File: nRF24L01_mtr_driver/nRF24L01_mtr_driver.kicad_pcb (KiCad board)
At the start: 2 copper layers, 77 x 47 mm, 121 parts, among them J1 Micro USB, J2 I/O, J4 VBAT, J5 MTR, J6 SERVO, J7 ICSP, Q1 AO4484, Q2 AO4484, Q3 AO4484, Q4 AO4484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

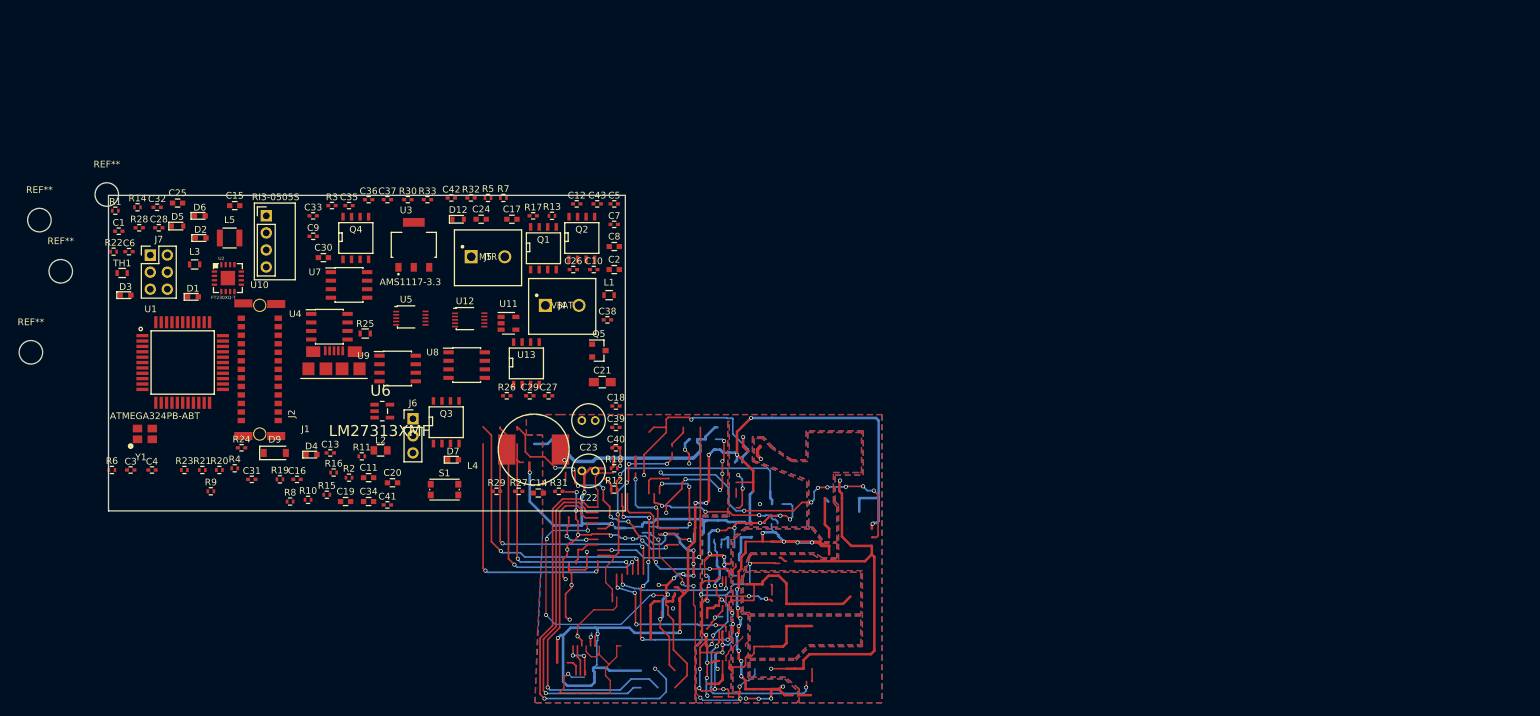
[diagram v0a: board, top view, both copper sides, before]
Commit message: added voltage sense isolation, needs routing
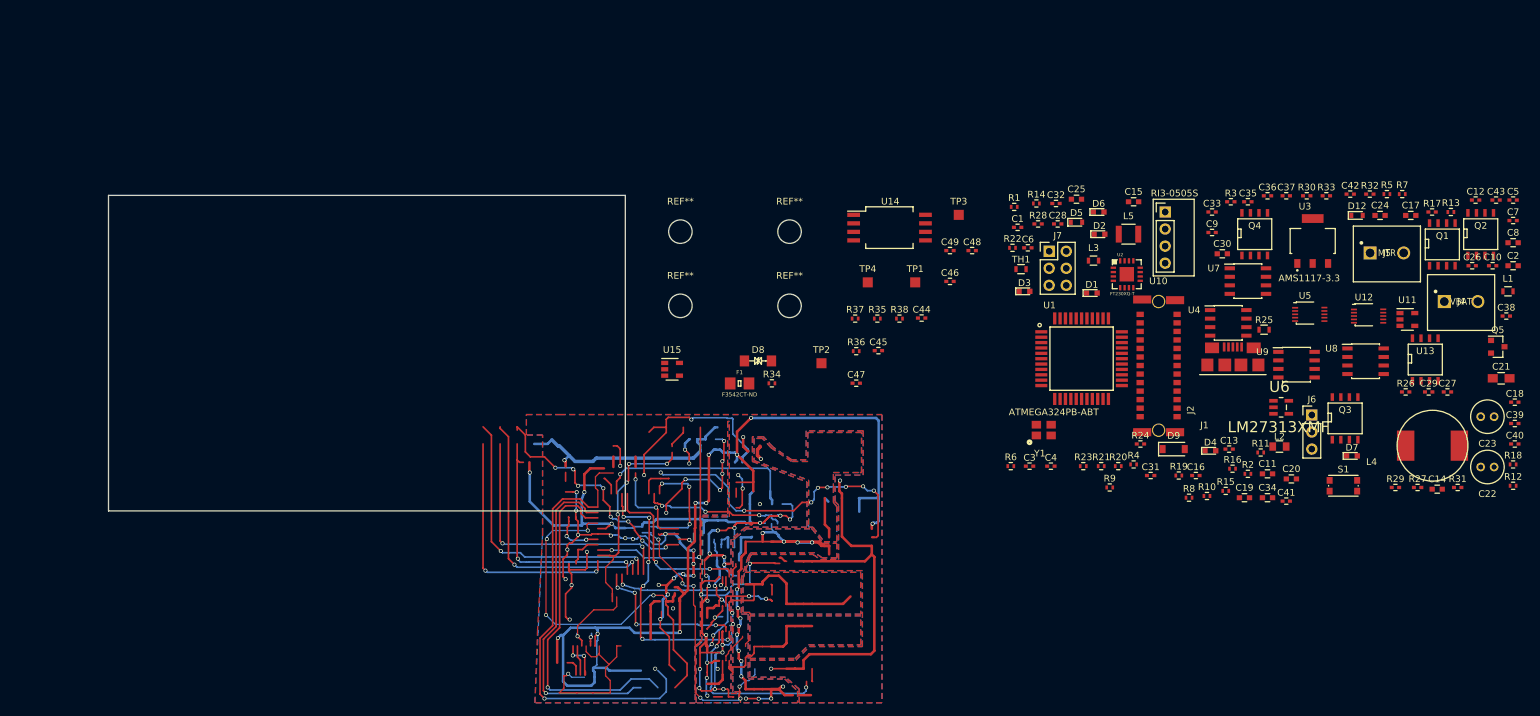
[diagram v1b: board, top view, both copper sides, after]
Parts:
- added C44: .1u, Capacitors_SMD:C_0402, F.Cu at (159.1, 60.7)
- added C45: .1u, Capacitors_SMD:C_0402, F.Cu at (152.6, 65.5)
- added C46: .1u, Capacitors_SMD:C_0402, F.Cu at (163.3, 55.2)
- added C47: .1u, Capacitors_SMD:C_0402, F.Cu at (149.3, 70.4)
- added C48: .1u, Capacitors_SMD:C_0402, F.Cu at (166.6, 50.6)
- added C49: .1u, Capacitors_SMD:C_0402, F.Cu at (163.3, 50.6)
- added D8: SMA6J18AHR3G, mc-footprints:DO-214AC, F.Cu at (132.7, 67.1)
- added F1: F3542CT-ND, Resistors:1206, F.Cu at (132.0, 70.4)
- added R34: 10k, Resistors_SMD:R_0402, F.Cu at (136.8, 70.4)
- added R35: 10k, Resistors_SMD:R_0402, F.Cu at (152.5, 60.8)
- added R36: 10k, Resistors_SMD:R_0402, F.Cu at (149.3, 65.6)
- added R37: 10k, Resistors_SMD:R_0402, F.Cu at (149.2, 60.8)
- added R38: 1k, Resistors_SMD:R_0402, F.Cu at (155.8, 60.8)
- added TP1: 5V0_PWR, Measurement_Points:Measurement_Point_Square-SMD-Pad_Small, F.Cu at (158.1, 55.4)
- added TP2: 12V_PWR, Measurement_Points:Measurement_Point_Square-SMD-Pad_Small, F.Cu at (144.1, 67.4)
- added TP3: 5V0_PWR, Measurement_Points:Measurement_Point_Square-SMD-Pad_Small, F.Cu at (164.6, 45.3)
- added TP4: 3V3_PWR, Measurement_Points:Measurement_Point_Square-SMD-Pad_Small, F.Cu at (151.0, 55.4)
- added U14: ACPL-C87A, Housings_SOIC:SSO-8_6.8x5.9mm_Pitch1.27mm_Clearance8mm, F.Cu at (154.3, 47.2)
- added U15: OPA237_SOT23-5, TO_SOT_Packages_SMD:SOT-23-5, F.Cu at (121.9, 68.3)
- R19: value 10k -> 100k
- R20: value 38k -> 12.7k
- moved C1 133.9 mm to (173.4, 47.2)
- moved C10 133.9 mm to (244.1, 52.9)
- moved C11 133.9 mm to (210.6, 83.9)
- moved C12 133.9 mm to (241.6, 43.1)
- moved C13 133.9 mm to (204.9, 80.2)
- moved C14 133.9 mm to (235.8, 86.2)
- moved C15 133.9 mm to (190.6, 43.4)
- moved C16 133.9 mm to (199.9, 84.1)
- moved C17 133.9 mm to (231.9, 45.4)
- moved C18 133.9 mm to (247.4, 73.2)
- moved C19 133.9 mm to (207.1, 87.4)
- moved C2 133.9 mm to (247.1, 52.9)
- moved C20 133.9 mm to (214.1, 84.6)
- moved C21 133.9 mm to (245.4, 69.7)
- moved C22 133.9 mm to (242.3, 82.9)
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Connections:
- C15 pad 1: /12V -> 12V_PWR
- C25 pad 1: /12V -> 12V_PWR
- C27 pad 1: /ADC1 -> Net-(C27-Pad1)
- C27 pad 2: GNDA -> GND_PWR
- C35 pad 2: /5V_MCU -> 5V0_MCU
- C36 pad 2: /5V_MCU -> 5V0_MCU
- C37 pad 2: /5V_MCU -> 5V0_MCU
- C38 pad 2: /5V_PWR -> 5V0_PWR
- C39 pad 2: /5V_PWR -> 5V0_PWR
- C40 pad 2: /5V_PWR -> 5V0_PWR
- D12 pad 2: /12V -> 12V_PWR
- D5 pad 2: /12V -> 12V_PWR
- J4 pad 1: VBAT -> Net-(F1-Pad2)
- R19 pad 1: /ADC1 -> VBAT
- R19 pad 2: GNDA -> Net-(C27-Pad1)
- R20 pad 1: /VBAT_S -> Net-(C27-Pad1)
- R20 pad 2: /ADC1 -> GND_PWR
- R5 pad 1: /12V -> 12V_PWR
- R6 pad 1: /3.3V -> 3V3_MCU
- R8 pad 1: /5V_mtr_driver -> 5V0_PWR
- U12 pad 1: /12V -> 12V_PWR
- U5 pad 1: /12V -> 12V_PWR
- U7 pad 1: /5V_MCU -> 5V0_MCU
- U7 pad 8: /5V_PWR -> 5V0_PWR
- U8 pad 1: /5V_MCU -> 5V0_MCU
- U8 pad 8: /5V_PWR -> 5V0_PWR
- U9 pad 1: /5V_MCU -> 5V0_MCU
- U9 pad 8: /5V_PWR -> 5V0_PWR
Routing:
- net (no net): track 1540.1 -> 1724.4 mm, vias 172 -> 181
- net Net-(C33-Pad1): track 81.4 -> 0.00 mm, vias 4 -> 0
- net VBAT: track 63.9 -> 0.00 mm, vias 3 -> 0
- net 5V0_PWR: track 35.1 -> 0.00 mm, vias 1 -> 0
- net /5V_PWR: track 3.78 -> 0.00 mm, vias 1 -> 0

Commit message: Changed the footprint of some 0603 cpacitors to 0402 to save space
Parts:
- C20, C30, C8: footprint Capacitors_SMD:C_0603 -> Capacitors_SMD:C_0402
- C21: footprint Capacitors_SMD:C_0805_HandSoldering -> Capacitors_SMD:C_0805
- R25: footprint Resistors_SMD:R_0603 -> Resistors_SMD:R_0402

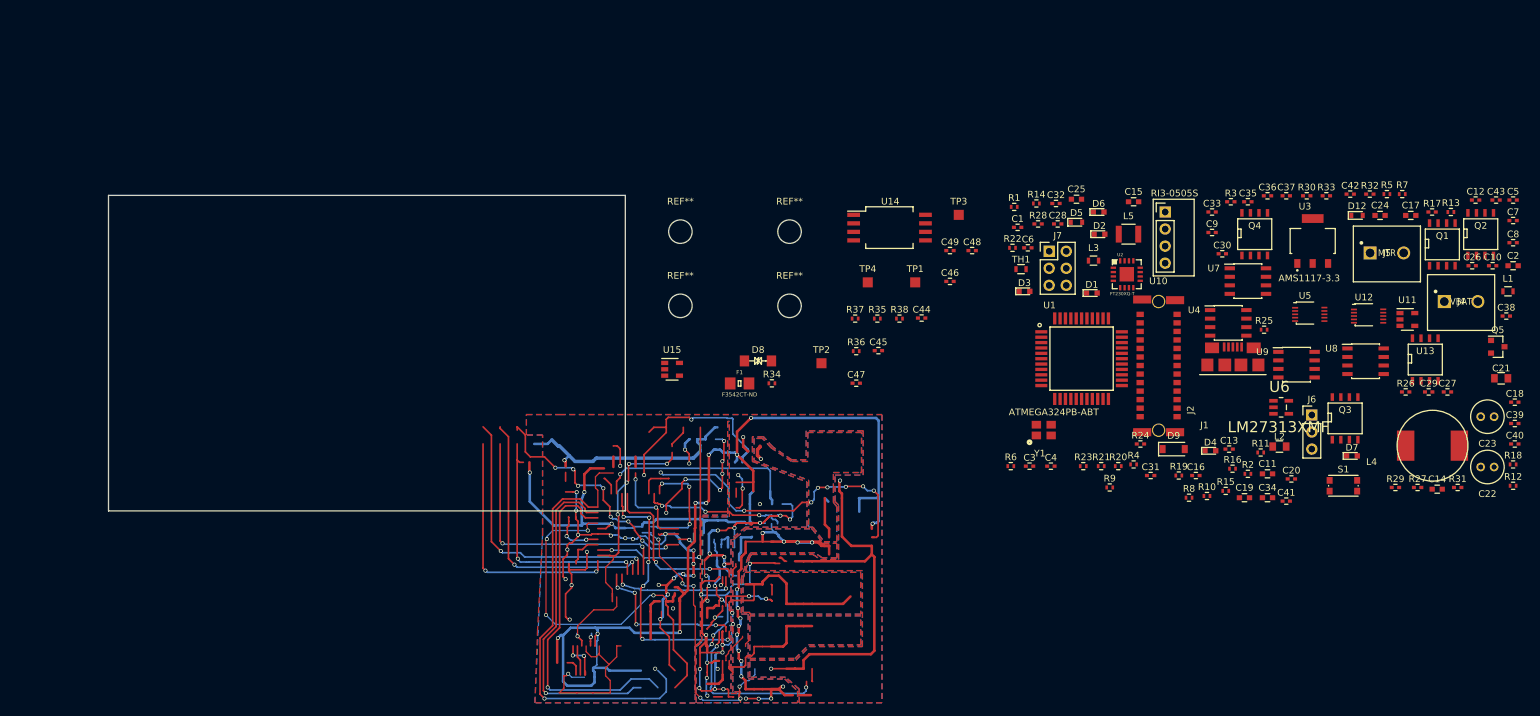
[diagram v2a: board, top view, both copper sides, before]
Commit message: placed major coponents, no routing
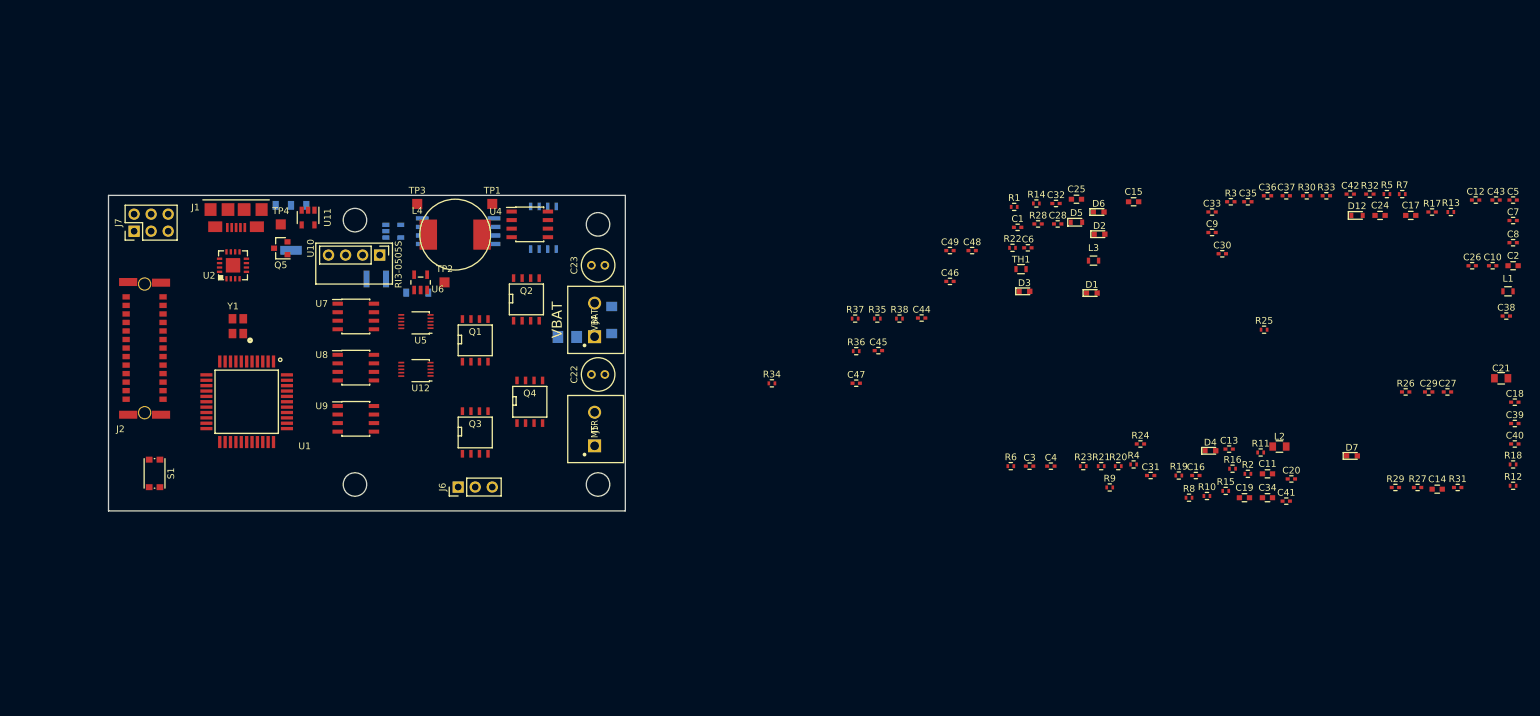
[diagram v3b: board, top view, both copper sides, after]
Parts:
- D8, D9, F1, L5, U13, U14, U15, U3: moved to B.Cu
- moved Q5 181.8 mm to (63.6, 50.3), turned to 180 degrees
- moved S1 177.0 mm to (44.8, 83.8), turned to 270 degrees
- moved U11 164.4 mm to (67.7, 45.7), turned to 270 degrees
- moved U3 152.2 mm to (65.2, 47.2)
- moved J2 151.0 mm to (46.1, 72.8)
- moved U8 150.4 mm to (74.8, 68.1)
- moved J1 147.2 mm to (60.1, 37.1), turned to 180 degrees
- moved Q1 144.7 mm to (92.6, 64.0)
- moved Q2 142.4 mm to (100.2, 57.9)
- moved L4 141.1 mm to (93.6, 48.3), turned to 180 degrees
- moved U12 140.7 mm to (84.5, 68.6), turned to 180 degrees
- moved U9 140.3 mm to (74.8, 75.7)
- moved J7 136.3 mm to (41.8, 47.8), turned to 90 degrees
- moved U2 133.1 mm to (56.5, 52.8), turned to 90 degrees
- moved U7 132.9 mm to (74.8, 60.5)
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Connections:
- D8 pad 1: GND_PWR -> Net-(D8-Pad1)
- F1 pad 2: Net-(F1-Pad2) -> Net-(D8-Pad1)
- J4 pad 1: Net-(F1-Pad2) -> Net-(D8-Pad1)
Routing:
- net (no net): track 1724.4 -> 0.00 mm, vias 181 -> 0
- removed copper zone on B.Cu, net /H1_out
- removed copper zone on F.Cu, net /H1_out
- removed copper zone on B.Cu, net /H2_out
- removed copper zone on F.Cu, net /H2_out
- removed copper zone on B.Cu, net /VBAT_S
- removed copper zone on F.Cu, net /VBAT_S
- removed copper zone on B.Cu, net GND_PWR
- removed copper zone on F.Cu, net GND_PWR
- removed copper zone on B.Cu, net VBAT
- removed copper zone on F.Cu, net VBAT
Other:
- board text added: "VBAT"
- board text removed: "5V"
- board text removed: "GND"
- board text removed: "PWM"

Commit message: placed most components
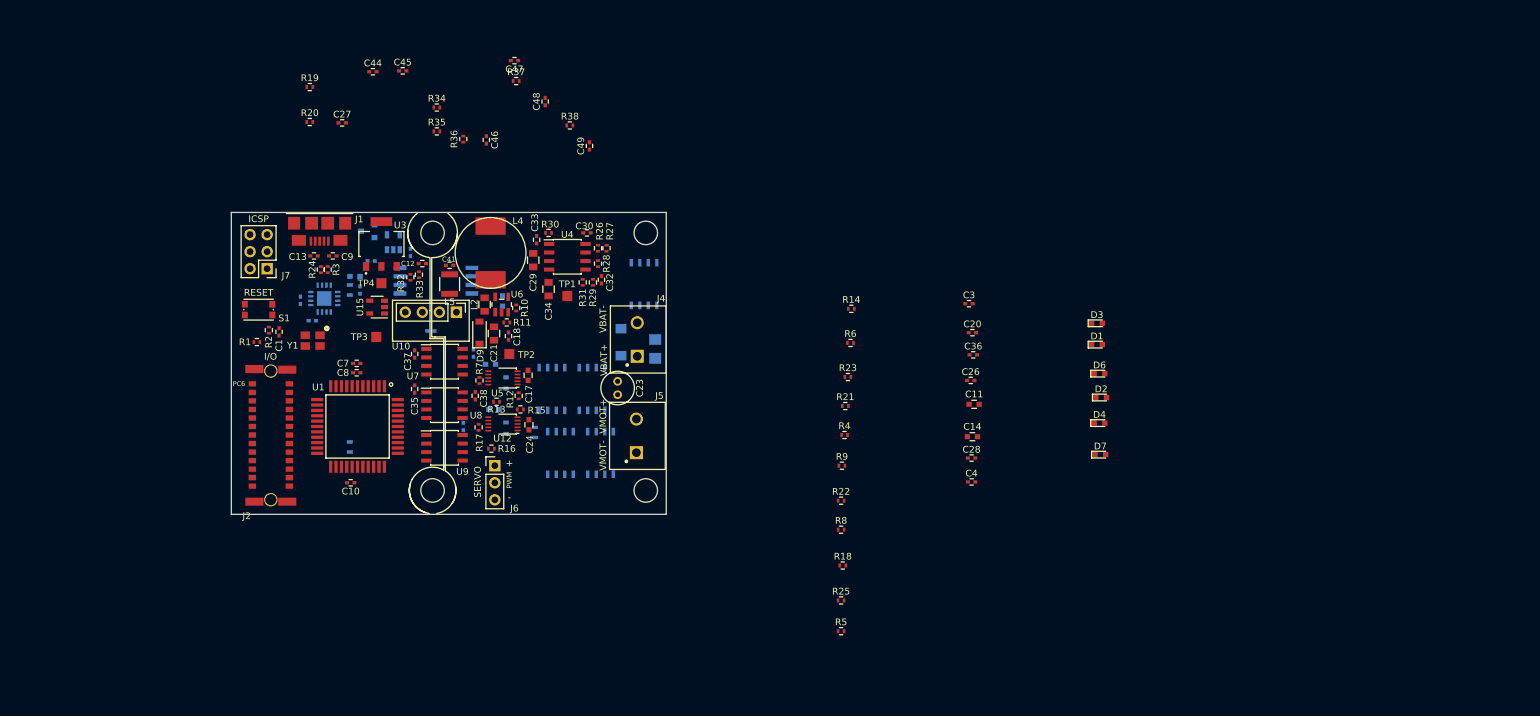
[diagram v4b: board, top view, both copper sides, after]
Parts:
- removed C22: 47u, D5mm_P2mm_cap:D5_P2_cap
- C15, C16, C19, C2, C25, C31, C39, C40, C42, C43, C5, C6, D12, D5, L1, L3, Q1, Q2, Q3, Q4, Q5, TH1, U11, U2: moved to B.Cu
- C29: footprint Capacitors_SMD:C_0402 -> Capacitors_SMD:C_0805
- C34: footprint Capacitors_SMD:C_0603 -> Capacitors_SMD:C_0805
- D9, L5, U15, U3: moved to F.Cu
- R17, R24, R26, R27, R28, R29, R3, R30, R31, R32, R33: footprint Capacitors_SMD:C_0402 -> Resistors_SMD:R_0402
- S1: value KMR231NG LFS -> RESET
- TP3: value 5V0_PWR -> 5V0_MCU
- TP4: value 3V3_PWR -> 3V3_MCU
- U12, U5: footprint footprints:VSSOP-8_2.4x2.1mm_Pitch0.5mm -> mc-footprints:VSSOP-8_2.4x2.1mm_Pitch0.5mm
- moved L1 174.0 mm to (73.9, 79.9), turned to 90 degrees
- moved C7 173.5 mm to (74.9, 67.4), turned to 180 degrees
- moved C8 173.3 mm to (74.9, 68.8), turned to 180 degrees
- moved C10 173.1 mm to (74.0, 85.2)
- moved C2 172.5 mm to (74.7, 54.5)
- moved C5 172.2 mm to (75.4, 56.5), turned to 270 degrees
- moved C27 169.4 mm to (72.8, 31.6)
- moved C43 161.9 mm to (82.9, 50.9), turned to 270 degrees
- moved C12 157.1 mm to (84.7, 52.6)
- moved C39 156.6 mm to (90.8, 76.8), turned to 270 degrees
- moved C40 155.7 mm to (92.3, 65.9), turned to 90 degrees
- moved C38 154.0 mm to (92.6, 72.3), turned to 90 degrees
- moved C18 150.2 mm to (97.5, 63.4), turned to 90 degrees
- moved C21 150.1 mm to (95.4, 63.0), turned to 90 degrees
- moved R12 148.7 mm to (99.1, 72.3), turned to 90 degrees
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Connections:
- C23 pad 1: VBAT -> Net-(C23-Pad1)
- C31 pad 1: /~RESET~ -> /~RESET
- C42 pad 1: VIN_MCU -> 5V0_MCU
- D8 pad 1: Net-(D8-Pad1) -> Net-(C23-Pad1)
- F1 pad 2: Net-(D8-Pad1) -> Net-(C23-Pad1)
- J4 pad 1: Net-(D8-Pad1) -> Net-(C23-Pad1)
- R32 pad 1: VIN_MCU -> 5V0_MCU
- U10 pad 4: VIN_MCU -> 5V0_MCU
- U13 pad 8: /5V -> 5V0_MCU
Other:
- board size 77 x 47 mm -> 64.8 x 45 mm
- board text added: "+"
- board text added: "-"
- board text added: "PC6"
- board text added: "PWM"
- board text added: "VBAT+"
- board text added: "VBAT-"
- board text added: "VMOT+"
- board text added: "VMOT-"
- board text added: "~"
- board text removed: "VBAT"

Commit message: 23 components left, stil needs routing
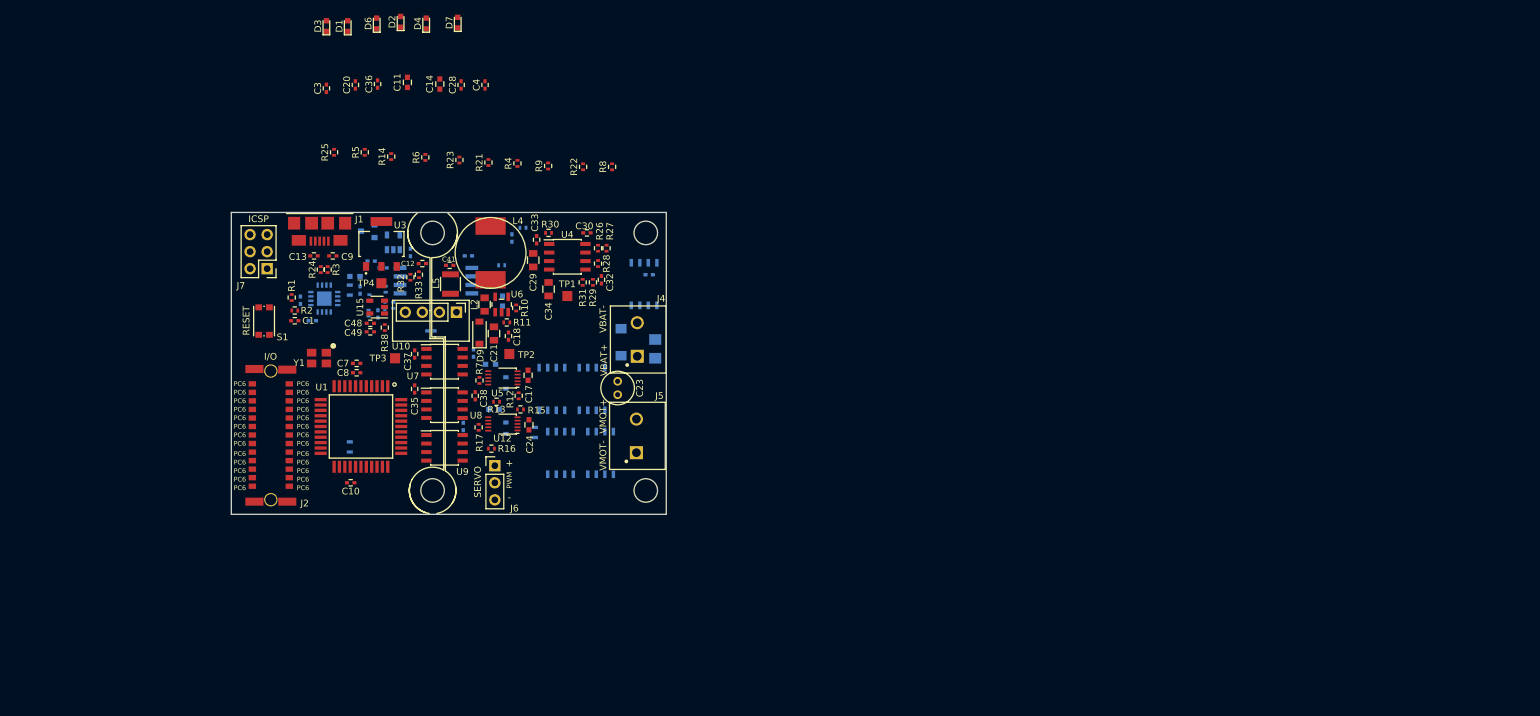
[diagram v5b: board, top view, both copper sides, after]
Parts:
- added C22: .1u, Capacitors_SMD:C_0402, B.Cu at (118.5, 54.2)
- C26, C27, C44, C45, C46, C47, R18, R19, R20, R34, R35, R36, R37: moved to B.Cu
- R8: value 1k -> q1k
- moved D3 123.0 mm to (70.4, 17.2), turned to 90 degrees
- moved D1 121.2 mm to (73.6, 17.2), turned to 90 degrees
- moved D6 119.6 mm to (77.9, 16.8), turned to 90 degrees
- moved D2 118.4 mm to (81.5, 16.6), turned to 90 degrees
- moved D4 116.6 mm to (85.3, 16.8), turned to 90 degrees
- moved D7 115.3 mm to (90.0, 16.7), turned to 90 degrees
- moved C3 100.9 mm to (70.4, 26.5), turned to 90 degrees
- moved R25 100.8 mm to (71.6, 36.0), turned to 90 degrees
- moved R5 100.6 mm to (76.1, 36.0), turned to 90 degrees
- moved C20 99.0 mm to (74.7, 26.0), turned to 90 degrees
- moved C36 97.4 mm to (78.0, 25.8), turned to 90 degrees
- moved C11 97.1 mm to (82.5, 25.6), turned to 90 degrees
- moved C14 95.1 mm to (87.3, 25.8), turned to 90 degrees
- moved C28 94.2 mm to (90.5, 26.0), turned to 90 degrees
- moved C4 93.5 mm to (94.0, 26.0), turned to 90 degrees
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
